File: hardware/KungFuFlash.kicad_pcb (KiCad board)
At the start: 2 copper layers, 60.6 x 62 mm, 40 parts, among them J1 USB Power, J2 USB_B_Micro, J4 SWD, Q1 BC817, SW1 Reset, SW2 Menu, SW3 Special, U1 C64-Exp-Port, U2 AMS1117-3.3, U3 STM32F405RGTx, Y1 8MHz

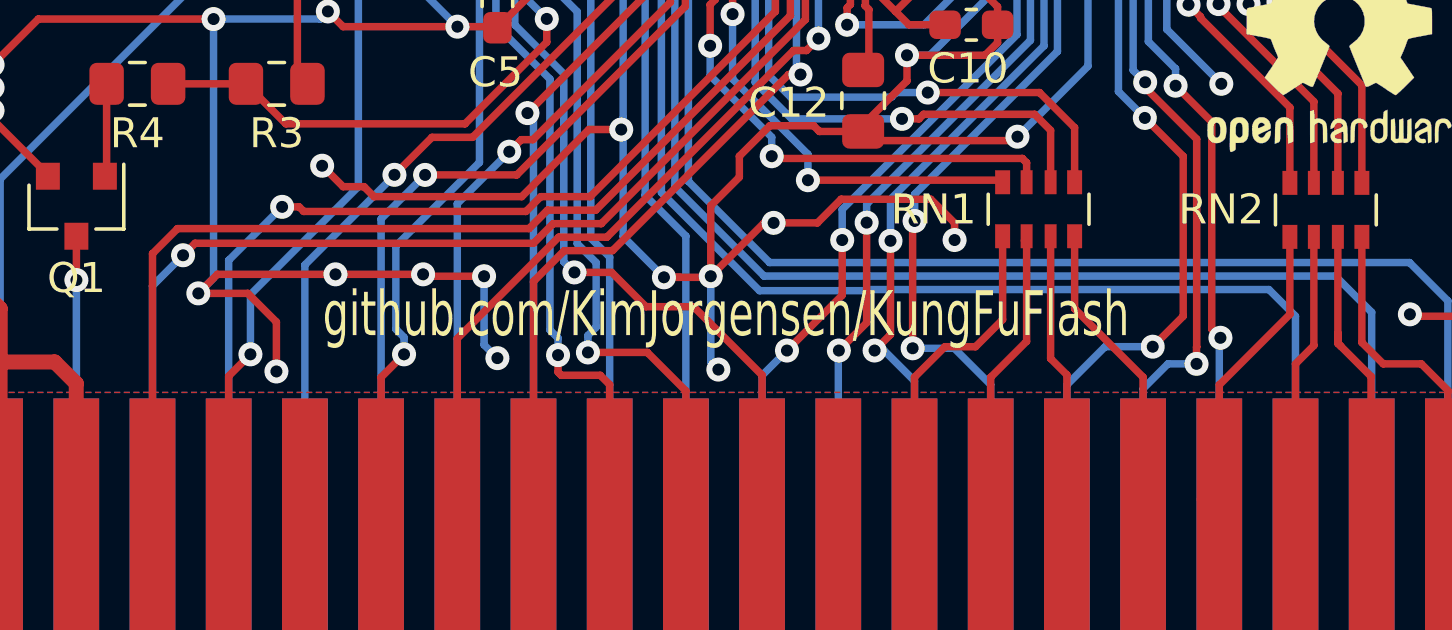
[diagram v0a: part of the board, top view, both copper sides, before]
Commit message: Move to Codeberg
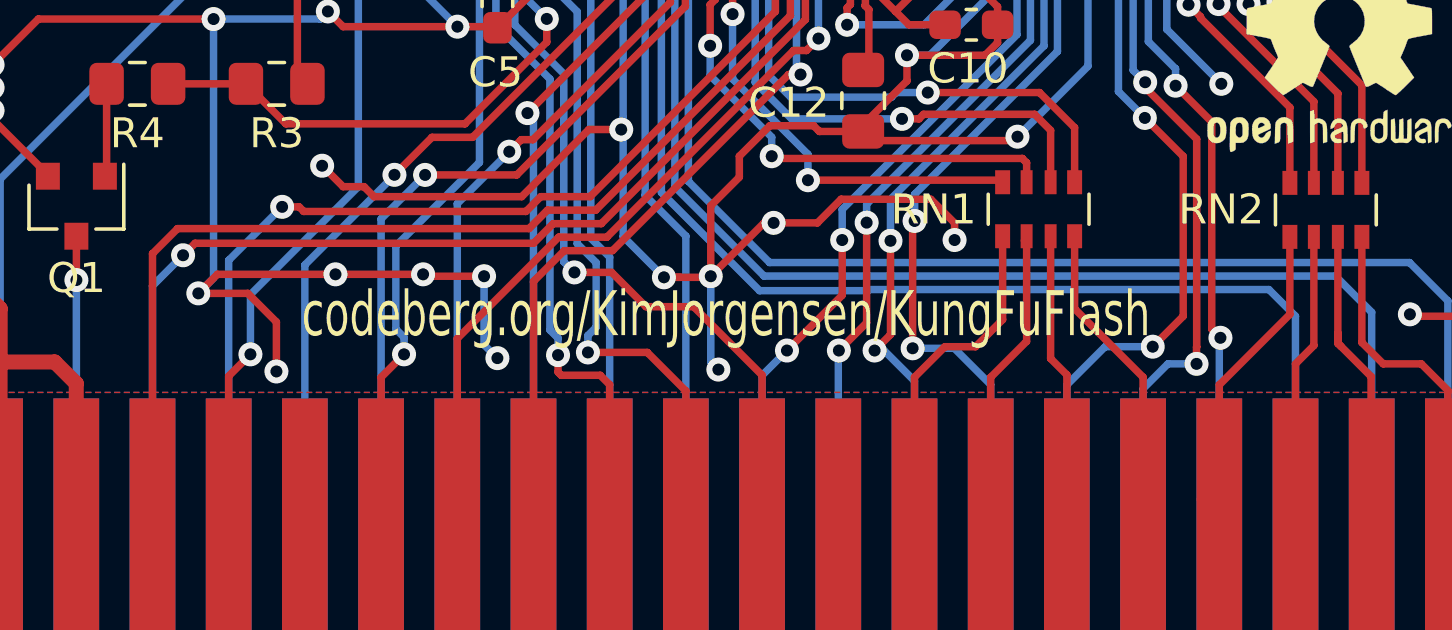
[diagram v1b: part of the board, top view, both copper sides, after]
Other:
- board text added: "codeberg.org/KimJorgensen/KungFuFlash"
- board text removed: "github.com/KimJorgensen/KungFuFlash"
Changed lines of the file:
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@@
   )
   (gr_circle (center 110.109 98.4885) (end 110.509 98.4885) (layer F.SilkS) (width 0.3))
-  (gr_text github.com/KimJorgensen/KungFuFlash (at 104.9655 119.3165) (layer F.SilkS)
+  (gr_text codeberg.org/KimJorgensen/KungFuFlash (at 104.9655 119.3165) (layer F.SilkS)
     (effects (font (size 1.5 1) (thickness 0.25)))
   )
